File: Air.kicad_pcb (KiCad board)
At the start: 2 copper layers, 91 x 55 mm, 106 parts, among them J1 AIR1, J10 USB_C_Receptacle_USB2.0_14P, J11 Conn_ST_STDC14, J12 CANR, J13 CAN, J14 CAN, J2 AIR2, J3 AIR3, J4 AIR4, J5 AIR5, J6 AIR6, J7 AIR7, J8 AIR8, J9 24V IN, Q1 2SC2712, Q2 2SC2712, Q3 2SC2712, Q4 2SC2712, Q5 2SC2712, Q6 2SC2712, Q7 2SC2712, Q8 2SC2712, SW1 NRST, U1 TLP293, U10 CH340E, U11 STM32F303K8Tx, U12 TJA1441, U2 TLP293, U3 TLP293, U4 TLP293, U5 TLP293, U6 TLP293, U7 TLP293, U8 TLP293, U9 NJM12877

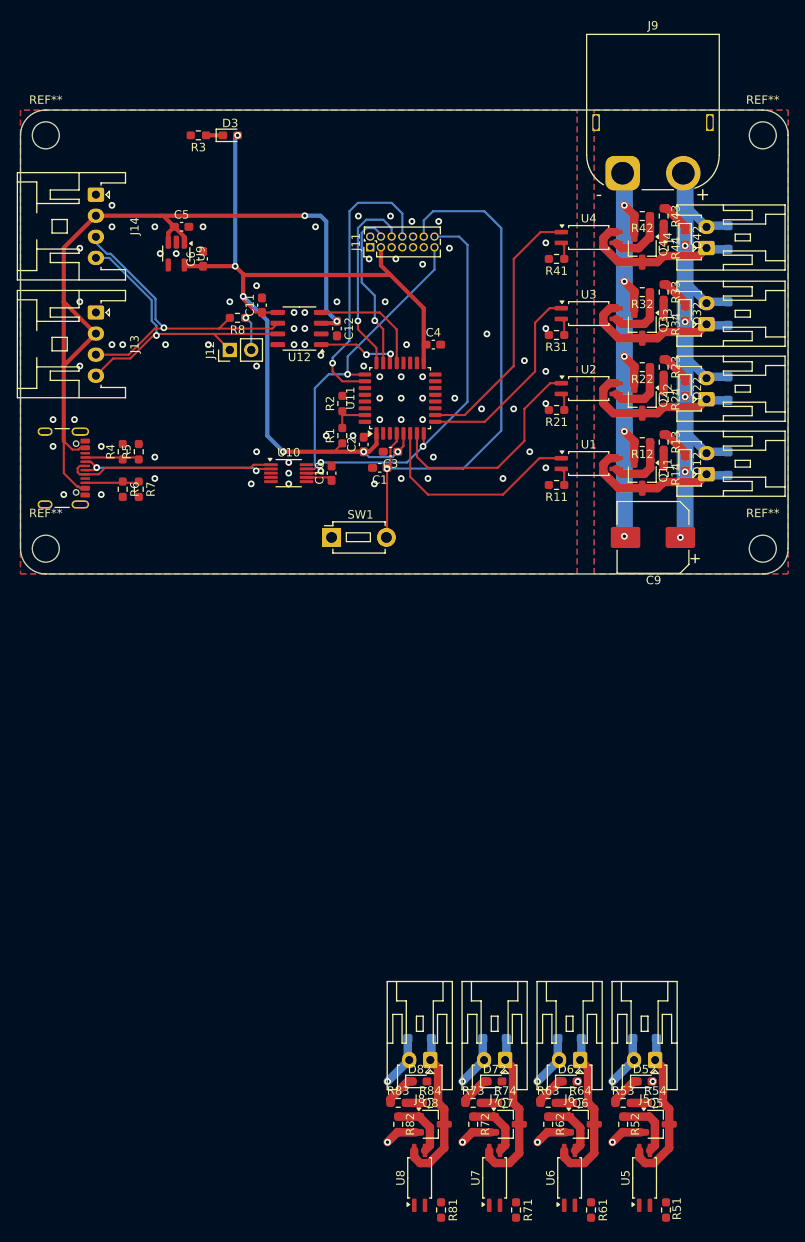
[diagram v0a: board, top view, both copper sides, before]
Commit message: feat: Update JST connector footprints in Drive and Air schematics
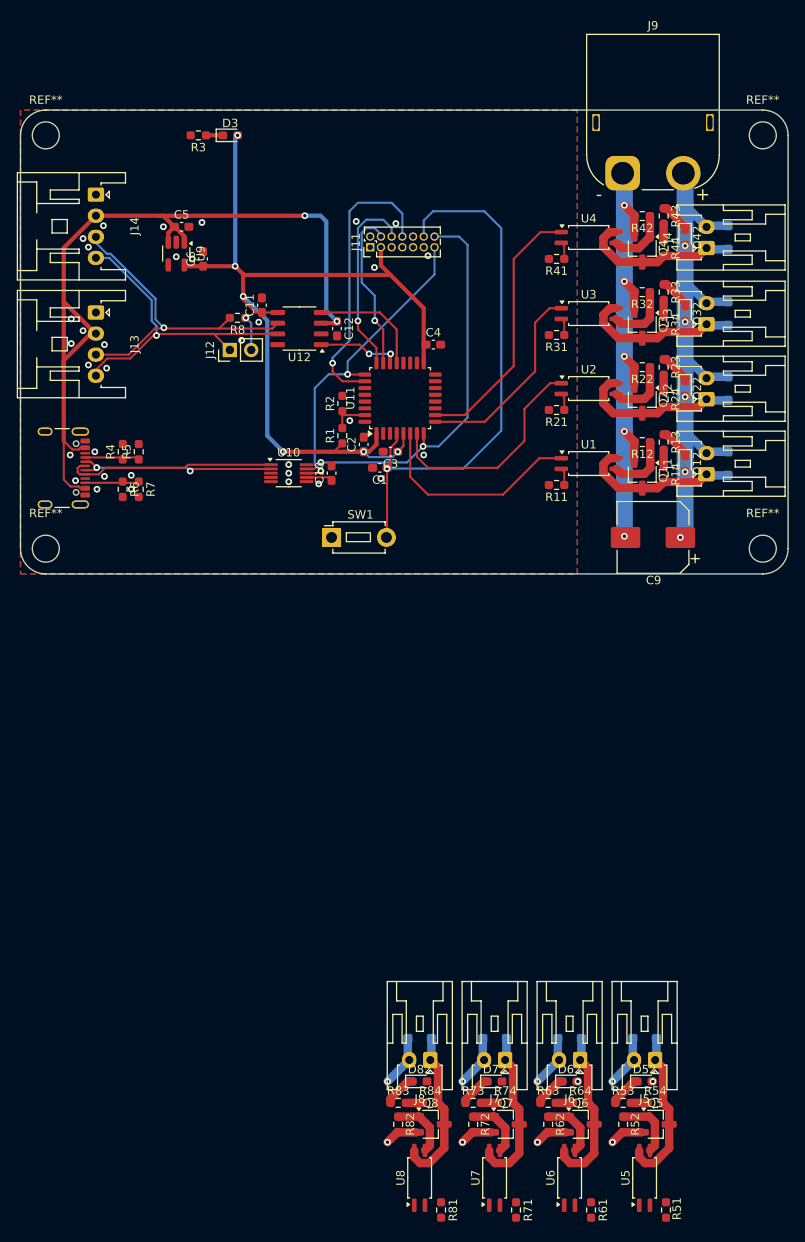
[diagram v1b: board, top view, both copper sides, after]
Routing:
- net /VCP_TX: track 46.9 -> 48.0 mm
- net +5V: track 97.8 -> 98.6 mm
- net GND: vias 76 -> 33
- removed copper zone on B.Cu, net GNDPWR
- removed copper zone on F.Cu, net GNDPWR

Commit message: feat: Update Air.kicad_pro configuration file with new sorting field and labels
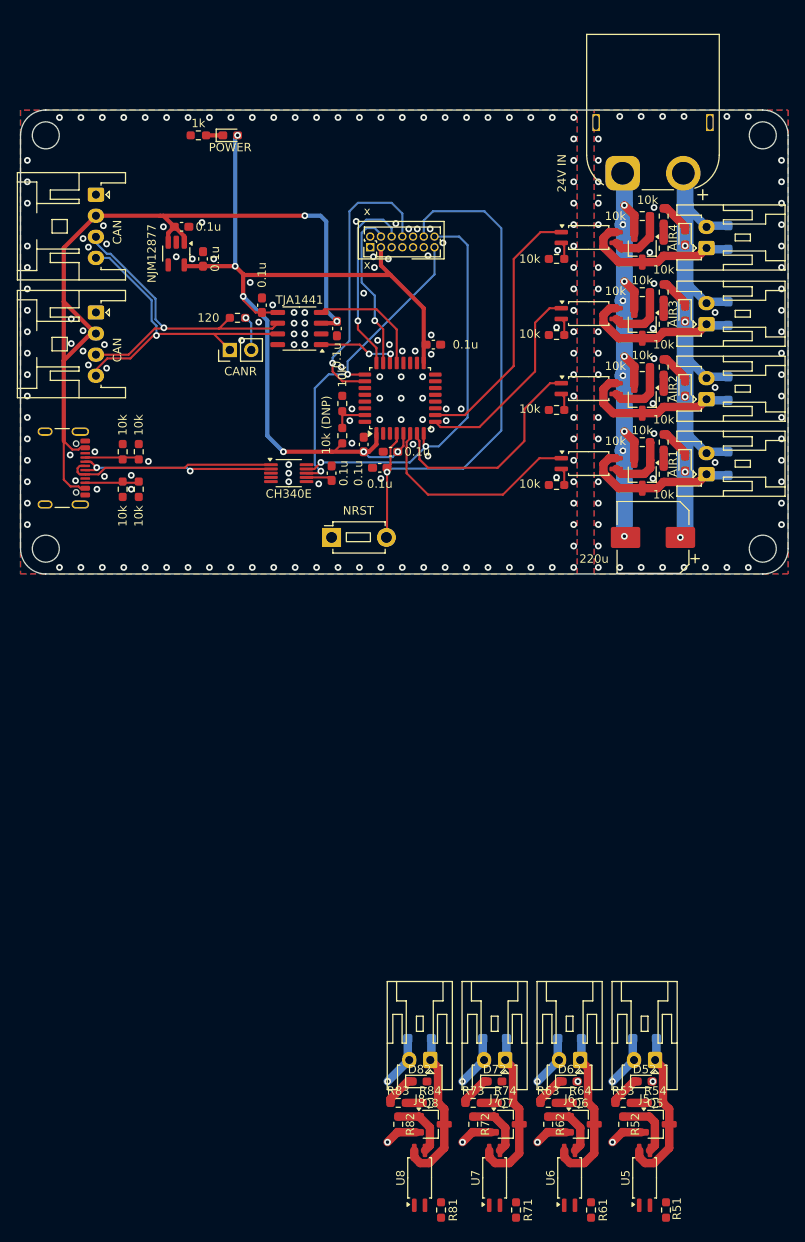
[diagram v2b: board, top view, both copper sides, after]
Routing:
- net /NRST: track 64.7 -> 65.3 mm
- net GNDPWR: track 74.4 -> 75.0 mm, vias 9 -> 72
- net /Drive/GPIO3: track 23.9 -> 24.4 mm
- net GND: vias 33 -> 167
- added copper zone on B.Cu, net GNDPWR
- added copper zone on F.Cu, net GNDPWR
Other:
- board text added: "x"
